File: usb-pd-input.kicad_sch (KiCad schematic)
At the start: 10 parts, among them J1 USB-C, U1 CH224D

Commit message: Update LCSC part numbers in schematics
Updated to match JLCPCB v1.1 order:
- J1: C2927029 → C456012 (USB-C connector)
- LED2: C72043 → C19171392 (Green 0603)
- LED3: C72041 → C5382145 (Blue 0603)
- R8: C17630 → C25623 (330Ω → 1kΩ)
- C31/C32/C33: C7393941 → C1710 (22nF)

Co-Authored-By: Claude Opus 4.5 <noreply@anthropic.com>
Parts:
- J1: LCSC Part C2927029 -> C456012
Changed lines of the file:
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@@
 			)
 		)
-		(property "LCSC Part" "C2927029"
+		(property "LCSC Part" "C456012"
 			(at 53.34 39.37 0)
 			(effects

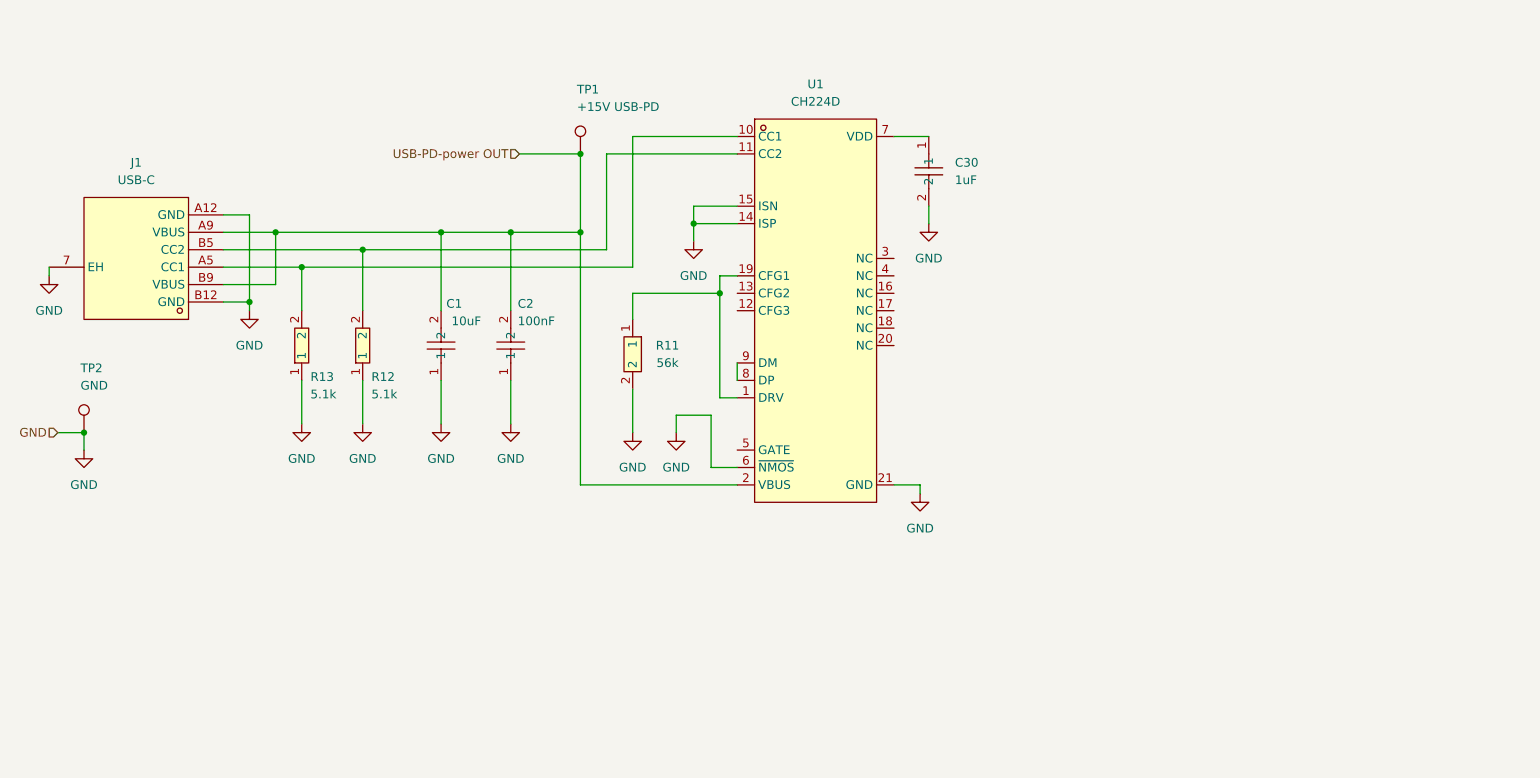
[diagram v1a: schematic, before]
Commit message: Update KiCad schematics for STUSB4500 v1.1 design
- Update USB-PD input stage with STUSB4500 + Q1 load switch
- Simplify output stage to single 16-pin connector (J2)
- Update FASTON terminal designators (J6-J9)

Co-Authored-By: Claude Opus 4.5 <noreply@anthropic.com>
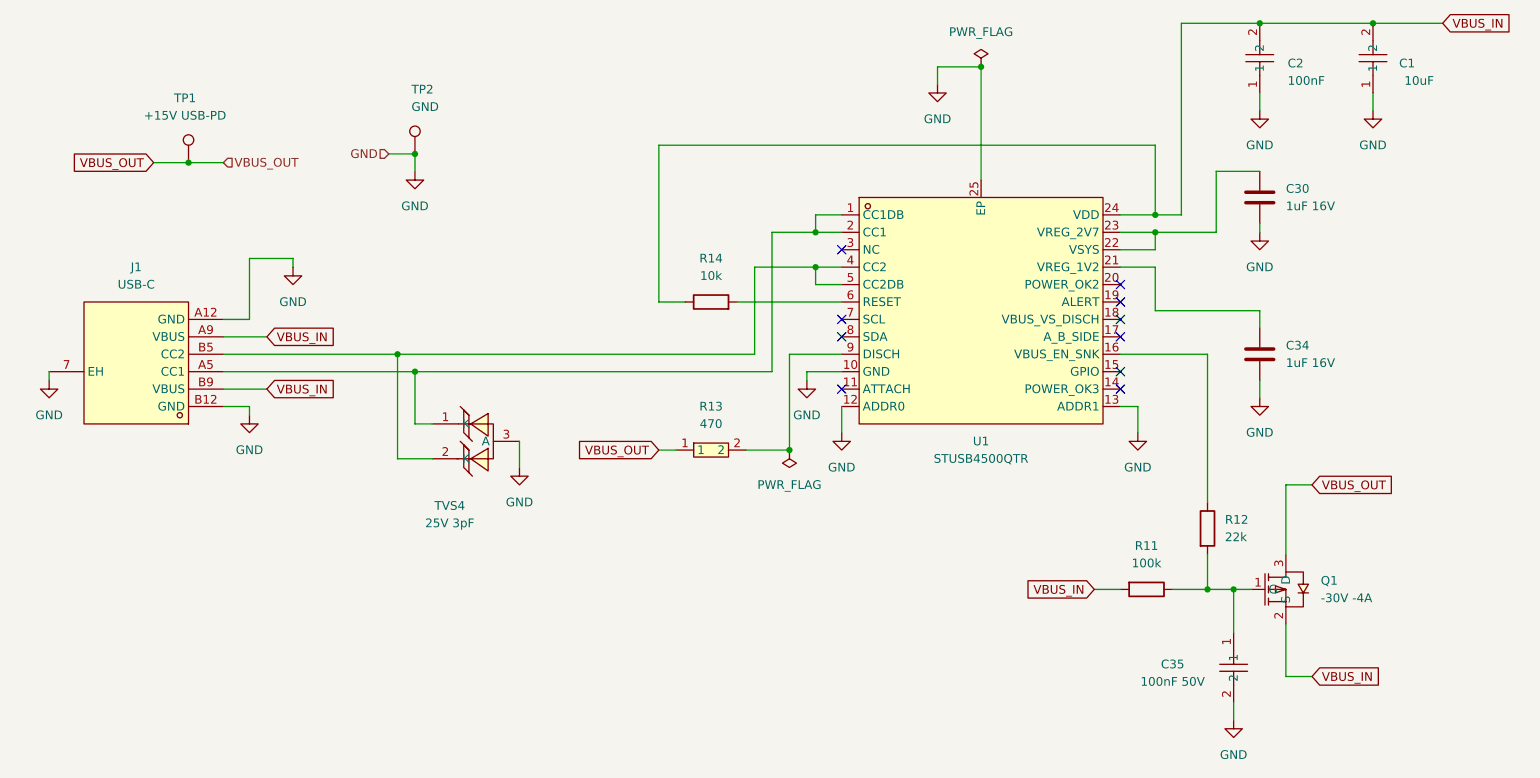
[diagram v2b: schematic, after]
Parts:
- removed C30: 1uF, zudo-pd:C0603, symbol zudo-pd:CGA0603X5R105K160JT
- removed R11: 56k, zudo-pd:R0603, symbol zudo-pd:RT0603BRD0756KL
- removed R12, R13: 5.1k, zudo-pd:R0603, symbol zudo-pd:0603WAF5101T5E
- removed U1: CH224D, zudo-pd:QFN-20_L3.0-W3.0-P0.40-BL-EP1.7, symbol zudo-pd:CH224D_C3975094
- added C30, C34: 1uF 16V, zudo-pd:C0603, symbol Device:C
- added C35: 100nF 50V, zudo-pd:C0805, symbol zudo-pd:CC0805KRX7R9BB104
- added Q1: -30V -4A, zudo-pd:SOT-23_L2.9-W1.3-P1.90-LS2.4-BR, symbol zudo-pd:AO3401A_C347476
- added R11: 100k, zudo-pd:R0603, symbol Device:R
- added R12: 22k, zudo-pd:R0603, symbol Device:R
- added R13: 470, zudo-pd:R0603, symbol zudo-pd:0603WAF4700T5E
- added R14: 10k, zudo-pd:R0603, symbol Device:R
- added TVS4: 25V 3pF, zudo-pd:SOT-23-3_L2.9-W1.6-P1.90-LS2.8-BR, symbol zudo-pd:ESDA25L_C343997
- added U1: STUSB4500QTR, zudo-pd:QFN-24_L4.0-W4.0-P0.50-BL-EP2.8, symbol zudo-pd:STUSB4500QTR
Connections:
- net GND: now also C30.2, C34.2, C35.2, TVS4.3 (A), U1.10 (GND), U1.12 (ADDR0), U1.13 (ADDR1), U1.25 (EP)
- net at J1.A5 (CC1): now also TVS4.1 (K), U1.1 (CC1DB), U1.2 (CC1)
- net at J1.B5 (CC2): now also TVS4.2 (K), U1.4 (CC2), U1.5 (CC2DB)
- net USB-PD-power OUT renamed VBUS_IN
- net VBUS_IN: now also Q1.2 (S), R11.2, R14.1, U1.24 (VDD); no longer TP1.1
- new net: C35.1, Q1.1 (G), R11.1, R12.2
- new net: R13.2, U1.9 (DISCH)
- new net: R14.2, U1.6 (RESET)
- new net: R12.1, U1.16 (VBUS_EN_SNK)
- new net: C34.1, U1.21 (VREG_1V2)
- new net: C30.1, U1.22 (VSYS), U1.23 (VREG_2V7)
- new net VBUS_OUT: Q1.3 (D), R13.1, TP1.1
- no-connect marks 0 -> 10
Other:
- moved on the sheet: C1, C2, J1, TP1, TP2
